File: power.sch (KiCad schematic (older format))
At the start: 35 parts, among them CN400 POWER_CONN, U108 74LS74A, U607 74LS08

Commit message: Associate more components
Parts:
- C400: value 470uF 16V -> 220uF 16V; footprint (none) -> Capacitor_THT:CP_Radial_D8.0mm_P5.00mm
- C403, C404, C405, C408, C410, C412, C420, C421, C422: footprint (none) -> Capacitor_THT:CP_Radial_D8.0mm_P5.00mm
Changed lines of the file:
@@
 P 1400 1700
 F 0 "C400" H 1518 1746 50  0000 L CNN
-F 1 "470uF 16V" H 1518 1655 50  0000 L CNN
-F 2 "" H 1438 1550 50  0001 C CNN
+F 1 "220uF 16V" H 1518 1655 50  0000 L CNN
+F 2 "Capacitor_THT:CP_Radial_D8.0mm_P5.00mm" H 1438 1550 50  0001 C CNN
 F 3 "~" H 1400 1700 50  0001 C CNN
 	1    1400 1700
@@
 F 0 "C403" H 3815 1746 50  0000 L CNN
 F 1 "47uF 16V" H 3815 1655 50  0000 L CNN
-F 2 "" H 3738 1550 50  0001 C CNN
+F 2 "Capacitor_THT:CP_Radial_D8.0mm_P5.00mm" H 3738 1550 50  0001 C CNN
 F 3 "~" H 3700 1700 50  0001 C CNN
 	1    3700 1700
@@
 F 0 "C404" H 4618 1746 50  0000 L CNN
 F 1 "47uF 16V" H 4618 1655 50  0000 L CNN
-F 2 "" H 4538 1550 50  0001 C CNN
+F 2 "Capacitor_THT:CP_Radial_D8.0mm_P5.00mm" H 4538 1550 50  0001 C CNN
 F 3 "~" H 4500 1700 50  0001 C CNN
 	1    4500 1700
@@
 F 0 "C405" H 5265 1746 50  0000 L CNN
 F 1 "47uF 16V" H 5265 1655 50  0000 L CNN
-F 2 "" H 5188 1550 50  0001 C CNN
+F 2 "Capacitor_THT:CP_Radial_D8.0mm_P5.00mm" H 5188 1550 50  0001 C CNN
 F 3 "~" H 5150 1700 50  0001 C CNN
 	1    5150 1700
@@
 F 0 "C408" H 3168 2146 50  0000 L CNN
 F 1 "47uF 16V" H 3168 2055 50  0000 L CNN
-F 2 "" H 3088 1950 50  0001 C CNN
+F 2 "Capacitor_THT:CP_Radial_D8.0mm_P5.00mm" H 3088 1950 50  0001 C CNN
 F 3 "~" H 3050 2100 50  0001 C CNN
 	1    3050 2100
@@
 F 0 "C410" H 4382 2054 50  0000 R CNN
 F 1 "47uF 16V" H 4382 2145 50  0000 R CNN
-F 2 "" H 4538 1950 50  0001 C CNN
+F 2 "Capacitor_THT:CP_Radial_D8.0mm_P5.00mm" H 4538 1950 50  0001 C CNN
 F 3 "~" H 4500 2100 50  0001 C CNN
 	1    4500 2100
@@
 F 0 "C412" H 5868 2146 50  0000 L CNN
 F 1 "47uF 16V" H 5868 2055 50  0000 L CNN
-F 2 "" H 5788 1950 50  0001 C CNN
+F 2 "Capacitor_THT:CP_Radial_D8.0mm_P5.00mm" H 5788 1950 50  0001 C CNN
 F 3 "~" H 5750 2100 50  0001 C CNN
 	1    5750 2100
@@
 F 0 "C420" H 5868 1746 50  0000 L CNN
 F 1 "47uF 16V" H 5868 1655 50  0000 L CNN
-F 2 "" H 5788 1550 50  0001 C CNN
+F 2 "Capacitor_THT:CP_Radial_D8.0mm_P5.00mm" H 5788 1550 50  0001 C CNN
 F 3 "~" H 5750 1700 50  0001 C CNN
 	1    5750 1700
@@
 F 0 "C421" H 6468 1746 50  0000 L CNN
 F 1 "47uF 16V" H 6468 1655 50  0000 L CNN
-F 2 "" H 6388 1550 50  0001 C CNN
+F 2 "Capacitor_THT:CP_Radial_D8.0mm_P5.00mm" H 6388 1550 50  0001 C CNN
 F 3 "~" H 6350 1700 50  0001 C CNN
 	1    6350 1700
@@
 F 0 "C422" H 7068 1746 50  0000 L CNN
 F 1 "47uF 16V" H 7068 1655 50  0000 L CNN
-F 2 "" H 6988 1550 50  0001 C CNN
+F 2 "Capacitor_THT:CP_Radial_D8.0mm_P5.00mm" H 6988 1550 50  0001 C CNN
 F 3 "~" H 6950 1700 50  0001 C CNN
 	1    6950 1700

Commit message: Update footprints
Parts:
- C401, C402, C407, C409, C411, C413, C414, C903, C906, C910: footprint (none) -> Capacitor_THT:C_Rect_L11.0mm_W2.8mm_P10.00mm_MKT
- C406: footprint (none) -> Capacitor_THT:CP_Radial_D8.0mm_P5.00mm
- CN400: footprint (none) -> d_amiga:A2K_PWR
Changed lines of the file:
@@
 F 0 "CN400" H 658 2881 50  0000 C CNN
 F 1 "POWER_CONN" H 658 2790 50  0000 C CNN
-F 2 "" H 550 2100 50  0001 C CNN
+F 2 "d_amiga:A2K_PWR" H 550 2100 50  0001 C CNN
 F 3 "~" H 550 2100 50  0001 C CNN
 F 4 "Male" H 550 2100 50  0001 C CNN "Gender"
@@
 F 0 "C401" H 2165 1746 50  0000 L CNN
 F 1 "0.01uF" H 2165 1655 50  0000 L CNN
-F 2 "" H 2088 1550 50  0001 C CNN
+F 2 "Capacitor_THT:C_Rect_L11.0mm_W2.8mm_P10.00mm_MKT" H 2088 1550 50  0001 C CNN
 F 3 "~" H 2050 1700 50  0001 C CNN
 	1    2050 1700
@@
 F 0 "C402" H 3168 1746 50  0000 L CNN
 F 1 "47uF 16V" H 3168 1655 50  0000 L CNN
-F 2 "" H 3088 1550 50  0001 C CNN
+F 2 "Capacitor_THT:C_Rect_L11.0mm_W2.8mm_P10.00mm_MKT" H 3088 1550 50  0001 C CNN
 F 3 "~" H 3050 1700 50  0001 C CNN
 	1    3050 1700
@@
 F 0 "C406" H 1282 2054 50  0000 R CNN
 F 1 "47uF 16V" H 1282 2145 50  0000 R CNN
-F 2 "" H 1438 1950 50  0001 C CNN
+F 2 "Capacitor_THT:CP_Radial_D8.0mm_P5.00mm" H 1438 1950 50  0001 C CNN
 F 3 "~" H 1400 2100 50  0001 C CNN
 	1    1400 2100
@@
 F 0 "C407" H 2165 2146 50  0000 L CNN
 F 1 "0.01uF" H 2165 2055 50  0000 L CNN
-F 2 "" H 2088 1950 50  0001 C CNN
+F 2 "Capacitor_THT:C_Rect_L11.0mm_W2.8mm_P10.00mm_MKT" H 2088 1950 50  0001 C CNN
 F 3 "~" H 2050 2100 50  0001 C CNN
 	1    2050 2100
@@
 F 0 "C409" H 3815 2146 50  0000 L CNN
 F 1 "0.01uF" H 3815 2055 50  0000 L CNN
-F 2 "" H 3738 1950 50  0001 C CNN
+F 2 "Capacitor_THT:C_Rect_L11.0mm_W2.8mm_P10.00mm_MKT" H 3738 1950 50  0001 C CNN
 F 3 "~" H 3700 2100 50  0001 C CNN
 	1    3700 2100
@@
 F 0 "C411" H 5265 2146 50  0000 L CNN
 F 1 "0.01uF" H 5265 2055 50  0000 L CNN
-F 2 "" H 5188 1950 50  0001 C CNN
+F 2 "Capacitor_THT:C_Rect_L11.0mm_W2.8mm_P10.00mm_MKT" H 5188 1950 50  0001 C CNN
 F 3 "~" H 5150 2100 50  0001 C CNN
 	1    5150 2100
@@
 F 0 "C413" H 6465 2146 50  0000 L CNN
 F 1 "0.01uF" H 6465 2055 50  0000 L CNN
-F 2 "" H 6388 1950 50  0001 C CNN
+F 2 "Capacitor_THT:C_Rect_L11.0mm_W2.8mm_P10.00mm_MKT" H 6388 1950 50  0001 C CNN
 F 3 "~" H 6350 2100 50  0001 C CNN
 	1    6350 2100
@@
 F 0 "C414" H 7065 2146 50  0000 L CNN
 F 1 "0.01uF" H 7065 2055 50  0000 L CNN
-F 2 "" H 6988 1950 50  0001 C CNN
+F 2 "Capacitor_THT:C_Rect_L11.0mm_W2.8mm_P10.00mm_MKT" H 6988 1950 50  0001 C CNN
 F 3 "~" H 6950 2100 50  0001 C CNN
 	1    6950 2100
@@
 F 0 "C903" H 7665 1746 50  0000 L CNN
 F 1 "0.1uF" H 7665 1655 50  0000 L CNN
-F 2 "" H 7588 1550 50  0001 C CNN
+F 2 "Capacitor_THT:C_Rect_L11.0mm_W2.8mm_P10.00mm_MKT" H 7588 1550 50  0001 C CNN
 F 3 "~" H 7550 1700 50  0001 C CNN
 	1    7550 1700
@@
 F 0 "C906" H 8115 1746 50  0000 L CNN
 F 1 "0.1uF" H 8115 1655 50  0000 L CNN
-F 2 "" H 8038 1550 50  0001 C CNN
+F 2 "Capacitor_THT:C_Rect_L11.0mm_W2.8mm_P10.00mm_MKT" H 8038 1550 50  0001 C CNN
 F 3 "~" H 8000 1700 50  0001 C CNN
 	1    8000 1700
@@
 F 0 "C910" H 8565 1746 50  0000 L CNN
 F 1 "0.1uF" H 8565 1655 50  0000 L CNN
-F 2 "" H 8488 1550 50  0001 C CNN
+F 2 "Capacitor_THT:C_Rect_L11.0mm_W2.8mm_P10.00mm_MKT" H 8488 1550 50  0001 C CNN
 F 3 "~" H 8450 1700 50  0001 C CNN
 	1    8450 1700

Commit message: Continue placing things
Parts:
- added H10, H11, H12, H13, H14: MountingHole_Pad, MountingHole:MountingHole_4mm_Pad_Via, symbol Mechanical:MountingHole_Pad
- C402: footprint Capacitor_THT:C_Rect_L11.0mm_W2.8mm_P10.00mm_MKT -> Capacitor_THT:CP_Radial_D8.0mm_P5.00mm
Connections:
- net GND: now also H10.1, H11.1, H12.1, H13.1, H14.1
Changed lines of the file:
@@
 F 0 "C402" H 3168 1746 50  0000 L CNN
 F 1 "47uF 16V" H 3168 1655 50  0000 L CNN
-F 2 "Capacitor_THT:C_Rect_L11.0mm_W2.8mm_P10.00mm_MKT" H 3088 1550 50  0001 C CNN
+F 2 "Capacitor_THT:CP_Radial_D8.0mm_P5.00mm" H 3088 1550 50  0001 C CNN
 F 3 "~" H 3050 1700 50  0001 C CNN
 	1    3050 1700
@@
 	2000 5900 1600 5900
 Wire Wire Line
-	2000 5900 2000 5400
+	2000 5900 2000 5650
 Wire Wire Line
 	2000 5400 1600 5400
 Wire Wire Line
-	2000 5400 2000 4900
+	2000 5400 2000 5150
 Connection ~ 2000 5400
 Connection ~ 2000 4900
@@
 	2000 4900 2400 4900
 Wire Wire Line
-	2000 4900 2000 4400
+	2000 4900 2000 4650
 Connection ~ 2000 4400
 Wire Wire Line
 	2000 4400 1600 4400
 Wire Wire Line
-	2000 4400 2000 3900
+	2000 4400 2000 4150
 Connection ~ 2000 3900
 Wire Wire Line
@@
 Text Notes 900  2400 0    50   ~ 0
 key
+$Comp
+L Mechanical:MountingHole_Pad H13
+U 1 1 5D27BD54
+P 2500 5400
+F 0 "H13" V 2500 5550 50  0000 L CNN
+F 1 "MountingHole_Pad" H 2600 5358 50  0001 L CNN
+F 2 "MountingHole:MountingHole_4mm_Pad_Via" H 2500 5400 50  0001 C CNN
+F 3 "~" H 2500 5400 50  0001 C CNN
+	1    2500 5400
+	0    1    1    0
+$EndComp
+Wire Wire Line
+	2000 5400 2400 5400
+$Comp
+L Mechanical:MountingHole_Pad H10
+U 1 1 5D281946
+P 2500 4150
+F 0 "H10" V 2500 4300 50  0000 L CNN
+F 1 "MountingHole_Pad" H 2600 4108 50  0001 L CNN
+F 2 "MountingHole:MountingHole_4mm_Pad_Via" H 2500 4150 50  0001 C CNN
+F 3 "~" H 2500 4150 50  0001 C CNN
+	1    2500 4150
+	0    1    1    0
+$EndComp
+$Comp
+L Mechanical:MountingHole_Pad H11
+U 1 1 5D281D87
+P 2500 4650
+F 0 "H11" V 2500 4800 50  0000 L CNN
+F 1 "MountingHole_Pad" H 2600 4608 50  0001 L CNN
+F 2 "MountingHole:MountingHole_4mm_Pad_Via" H 2500 4650 50  0001 C CNN
+F 3 "~" H 2500 4650 50  0001 C CNN
+	1    2500 4650
+	0    1    1    0
+$EndComp
+$Comp
+L Mechanical:MountingHole_Pad H12
+U 1 1 5D2822E5
+P 2500 5150
+F 0 "H12" V 2500 5300 50  0000 L CNN
+F 1 "MountingHole_Pad" H 2600 5108 50  0001 L CNN
+F 2 "MountingHole:MountingHole_4mm_Pad_Via" H 2500 5150 50  0001 C CNN
+F 3 "~" H 2500 5150 50  0001 C CNN
+	1    2500 5150
+	0    1    1    0
+$EndComp
+$Comp
+L Mechanical:MountingHole_Pad H14
+U 1 1 5D282642
+P 2500 5650
+F 0 "H14" V 2500 5800 50  0000 L CNN
+F 1 "MountingHole_Pad" H 2600 5608 50  0001 L CNN
+F 2 "MountingHole:MountingHole_4mm_Pad_Via" H 2500 5650 50  0001 C CNN
+F 3 "~" H 2500 5650 50  0001 C CNN
+	1    2500 5650
+	0    1    1    0
+$EndComp
+Wire Wire Line
+	2400 5650 2000 5650
+Connection ~ 2000 5650
+Wire Wire Line
+	2000 5650 2000 5400
+Wire Wire Line
+	2000 5150 2400 5150
+Connection ~ 2000 5150
+Wire Wire Line
+	2000 5150 2000 4900
+Wire Wire Line
+	2400 4650 2000 4650
+Connection ~ 2000 4650
+Wire Wire Line
+	2000 4650 2000 4400
+Wire Wire Line
+	2000 4150 2400 4150
+Connection ~ 2000 4150
+Wire Wire Line
+	2000 4150 2000 3900
 $EndSCHEMATC

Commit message: first placement pass is done
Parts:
- added FB904, FB906: Ferrite_Bead, Inductor_THT:L_Axial_L7.0mm_D3.3mm_P5.08mm_Vertical_Fastron_MICC, symbol Device:Ferrite_Bead
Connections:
- net GND: now also FB904.1, FB904.2, FB906.1, FB906.2
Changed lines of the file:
@@
 Wire Wire Line
 	2000 4150 2000 3900
+$Comp
+L Device:Ferrite_Bead FB904
+U 1 1 5DDC1F23
+P 5000 4150
+F 0 "FB904" H 5137 4150 50  0000 L CNN
+F 1 "Ferrite_Bead" H 5137 4105 50  0001 L CNN
+F 2 "Inductor_THT:L_Axial_L7.0mm_D3.3mm_P5.08mm_Vertical_Fastron_MICC" V 4930 4150 50  0001 C CNN
+F 3 "~" H 5000 4150 50  0001 C CNN
+	1    5000 4150
+	1    0    0    -1
+$EndComp
+$Comp
+L Device:Ferrite_Bead FB906
+U 1 1 5DDC28AE
+P 6000 4150
+F 0 "FB906" H 6137 4150 50  0000 L CNN
+F 1 "Ferrite_Bead" H 6137 4105 50  0001 L CNN
+F 2 "Inductor_THT:L_Axial_L7.0mm_D3.3mm_P5.08mm_Vertical_Fastron_MICC" V 5930 4150 50  0001 C CNN
+F 3 "~" H 6000 4150 50  0001 C CNN
+	1    6000 4150
+	1    0    0    -1
+$EndComp
+$Comp
+L power:GND #PWR0272
+U 1 1 5DDC360A
+P 5500 4500
+F 0 "#PWR0272" H 5500 4250 50  0001 C CNN
+F 1 "GND" H 5505 4327 50  0000 C CNN
+F 2 "" H 5500 4500 50  0001 C CNN
+F 3 "" H 5500 4500 50  0001 C CNN
+	1    5500 4500
+	1    0    0    -1
+$EndComp
+Wire Wire Line
+	5000 4000 5000 3750
+Wire Wire Line
+	5000 3750 5500 3750
+Wire Wire Line
+	5500 3750 5500 4350
+Wire Wire Line
+	6000 4000 6000 3750
+Wire Wire Line
+	6000 3750 5500 3750
+Connection ~ 5500 3750
+Wire Wire Line
+	5000 4300 5000 4350
+Wire Wire Line
+	5000 4350 5500 4350
+Connection ~ 5500 4350
+Wire Wire Line
+	5500 4350 5500 4500
+Wire Wire Line
+	5500 4350 6000 4350
+Wire Wire Line
+	6000 4350 6000 4300
 $EndSCHEMATC

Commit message: Make caps footprint smaller
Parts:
- C401, C407, C409, C411, C413, C414, C903, C906, C910: footprint Capacitor_THT:C_Rect_L11.0mm_W2.8mm_P10.00mm_MKT -> Capacitor_THT:C_Rect_L11.5mm_W2.0mm_P10.00mm_MKT
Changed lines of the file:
@@
 F 0 "C401" H 2165 1746 50  0000 L CNN
 F 1 "0.01uF" H 2165 1655 50  0000 L CNN
-F 2 "Capacitor_THT:C_Rect_L11.0mm_W2.8mm_P10.00mm_MKT" H 2088 1550 50  0001 C CNN
+F 2 "Capacitor_THT:C_Rect_L11.5mm_W2.0mm_P10.00mm_MKT" H 2088 1550 50  0001 C CNN
 F 3 "~" H 2050 1700 50  0001 C CNN
 	1    2050 1700
@@
 F 0 "C407" H 2165 2146 50  0000 L CNN
 F 1 "0.01uF" H 2165 2055 50  0000 L CNN
-F 2 "Capacitor_THT:C_Rect_L11.0mm_W2.8mm_P10.00mm_MKT" H 2088 1950 50  0001 C CNN
+F 2 "Capacitor_THT:C_Rect_L11.5mm_W2.0mm_P10.00mm_MKT" H 2088 1950 50  0001 C CNN
 F 3 "~" H 2050 2100 50  0001 C CNN
 	1    2050 2100
@@
 F 0 "C409" H 3815 2146 50  0000 L CNN
 F 1 "0.01uF" H 3815 2055 50  0000 L CNN
-F 2 "Capacitor_THT:C_Rect_L11.0mm_W2.8mm_P10.00mm_MKT" H 3738 1950 50  0001 C CNN
+F 2 "Capacitor_THT:C_Rect_L11.5mm_W2.0mm_P10.00mm_MKT" H 3738 1950 50  0001 C CNN
 F 3 "~" H 3700 2100 50  0001 C CNN
 	1    3700 2100
@@
 F 0 "C411" H 5265 2146 50  0000 L CNN
 F 1 "0.01uF" H 5265 2055 50  0000 L CNN
-F 2 "Capacitor_THT:C_Rect_L11.0mm_W2.8mm_P10.00mm_MKT" H 5188 1950 50  0001 C CNN
+F 2 "Capacitor_THT:C_Rect_L11.5mm_W2.0mm_P10.00mm_MKT" H 5188 1950 50  0001 C CNN
 F 3 "~" H 5150 2100 50  0001 C CNN
 	1    5150 2100
@@
 F 0 "C413" H 6465 2146 50  0000 L CNN
 F 1 "0.01uF" H 6465 2055 50  0000 L CNN
-F 2 "Capacitor_THT:C_Rect_L11.0mm_W2.8mm_P10.00mm_MKT" H 6388 1950 50  0001 C CNN
+F 2 "Capacitor_THT:C_Rect_L11.5mm_W2.0mm_P10.00mm_MKT" H 6388 1950 50  0001 C CNN
 F 3 "~" H 6350 2100 50  0001 C CNN
 	1    6350 2100
@@
 F 0 "C414" H 7065 2146 50  0000 L CNN
 F 1 "0.01uF" H 7065 2055 50  0000 L CNN
-F 2 "Capacitor_THT:C_Rect_L11.0mm_W2.8mm_P10.00mm_MKT" H 6988 1950 50  0001 C CNN
+F 2 "Capacitor_THT:C_Rect_L11.5mm_W2.0mm_P10.00mm_MKT" H 6988 1950 50  0001 C CNN
 F 3 "~" H 6950 2100 50  0001 C CNN
 	1    6950 2100
@@
 F 0 "C903" H 7665 1746 50  0000 L CNN
 F 1 "0.1uF" H 7665 1655 50  0000 L CNN
-F 2 "Capacitor_THT:C_Rect_L11.0mm_W2.8mm_P10.00mm_MKT" H 7588 1550 50  0001 C CNN
+F 2 "Capacitor_THT:C_Rect_L11.5mm_W2.0mm_P10.00mm_MKT" H 7588 1550 50  0001 C CNN
 F 3 "~" H 7550 1700 50  0001 C CNN
 	1    7550 1700
@@
 F 0 "C906" H 8115 1746 50  0000 L CNN
 F 1 "0.1uF" H 8115 1655 50  0000 L CNN
-F 2 "Capacitor_THT:C_Rect_L11.0mm_W2.8mm_P10.00mm_MKT" H 8038 1550 50  0001 C CNN
+F 2 "Capacitor_THT:C_Rect_L11.5mm_W2.0mm_P10.00mm_MKT" H 8038 1550 50  0001 C CNN
 F 3 "~" H 8000 1700 50  0001 C CNN
 	1    8000 1700
@@
 F 0 "C910" H 8565 1746 50  0000 L CNN
 F 1 "0.1uF" H 8565 1655 50  0000 L CNN
-F 2 "Capacitor_THT:C_Rect_L11.0mm_W2.8mm_P10.00mm_MKT" H 8488 1550 50  0001 C CNN
+F 2 "Capacitor_THT:C_Rect_L11.5mm_W2.0mm_P10.00mm_MKT" H 8488 1550 50  0001 C CNN
 F 3 "~" H 8450 1700 50  0001 C CNN
 	1    8450 1700

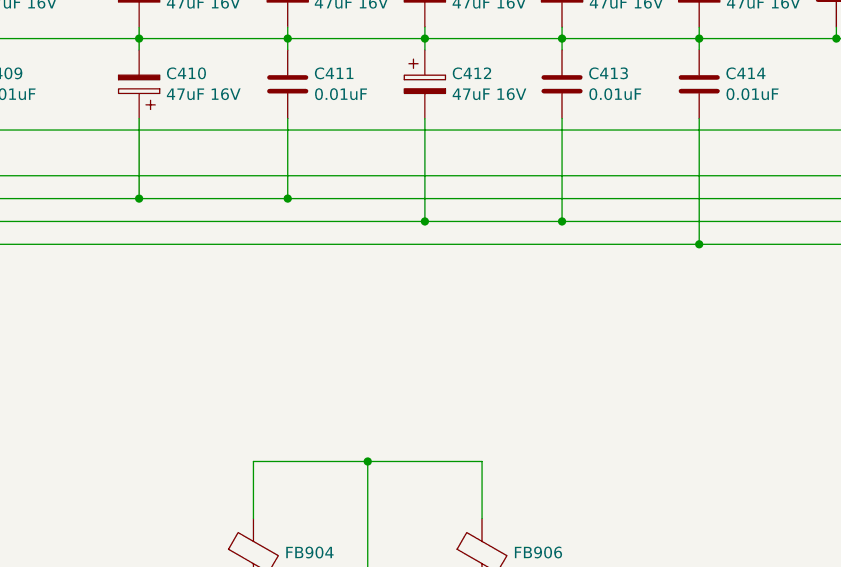
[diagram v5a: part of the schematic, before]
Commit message: Correct some components orientation
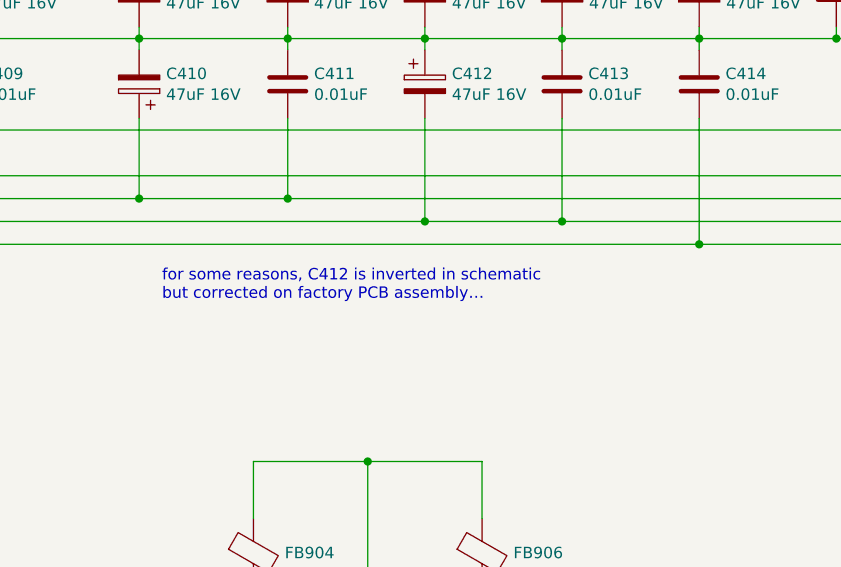
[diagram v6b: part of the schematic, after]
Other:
- note added: "for some reasons, C412 is inverted in schematic\nbut corrected on factory PCB assembly…"
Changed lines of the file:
@@
 Wire Wire Line
 	6000 4350 6000 4300
+Text Notes 4600 3050 0    50   ~ 0
+for some reasons, C412 is inverted in schematic\nbut corrected on factory PCB assembly…
 $EndSCHEMATC

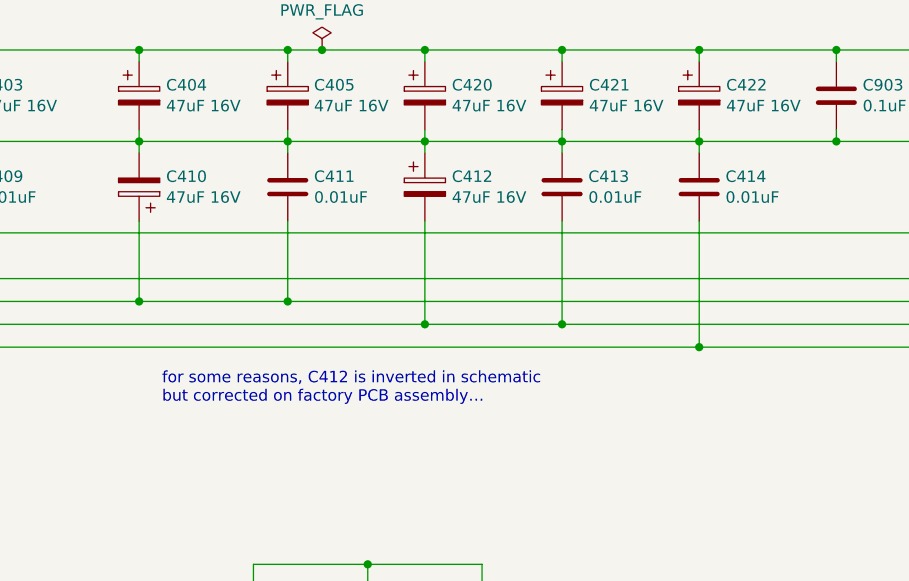
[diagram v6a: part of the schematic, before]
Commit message: Fix capacitor error; regen files
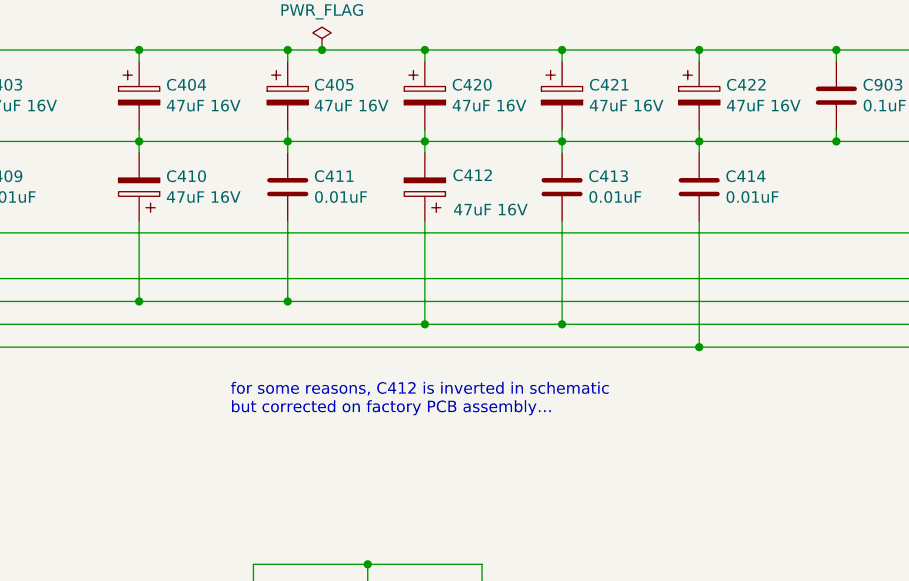
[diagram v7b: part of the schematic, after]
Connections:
- net -5V: now also C412.1; no longer C412.2
- net GND: now also C412.2; no longer C412.1
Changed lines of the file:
@@
 U 1 1 5DDDF78A
 P 5750 2100
-F 0 "C412" H 5868 2146 50  0000 L CNN
-F 1 "47uF 16V" H 5868 2055 50  0000 L CNN
+F 0 "C412" H 5450 2050 50  0000 L CNN
+F 1 "47uF 16V" H 5300 2200 50  0000 L CNN
 F 2 "Capacitor_THT:CP_Radial_D8.0mm_P5.00mm" H 5788 1950 50  0001 C CNN
 F 3 "~" H 5750 2100 50  0001 C CNN
 	1    5750 2100
-	1    0    0    -1
+	-1   0    0    1
 $EndComp
 $Comp
@@
 Wire Wire Line
 	6000 4350 6000 4300
-Text Notes 4600 3050 0    50   ~ 0
+Text Notes 4900 3100 0    50   ~ 0
 for some reasons, C412 is inverted in schematic\nbut corrected on factory PCB assembly…
 $EndSCHEMATC

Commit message: Add DoNotPopulate field for components which shouldn't be fitted
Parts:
- FB904, FB906: DoNotPopulate (none) -> yes
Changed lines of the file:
@@
 F 2 "Inductor_THT:L_Axial_L7.0mm_D3.3mm_P5.08mm_Vertical_Fastron_MICC" V 4930 4150 50  0001 C CNN
 F 3 "~" H 5000 4150 50  0001 C CNN
+F 4 "yes" H 5000 4150 50  0001 C CNN "DoNotPopulate"
 	1    5000 4150
 	1    0    0    -1
@@
 F 2 "Inductor_THT:L_Axial_L7.0mm_D3.3mm_P5.08mm_Vertical_Fastron_MICC" V 5930 4150 50  0001 C CNN
 F 3 "~" H 6000 4150 50  0001 C CNN
+F 4 "yes" H 6000 4150 50  0001 C CNN "DoNotPopulate"
 	1    6000 4150
 	1    0    0    -1
